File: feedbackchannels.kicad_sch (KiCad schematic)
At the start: 75 parts

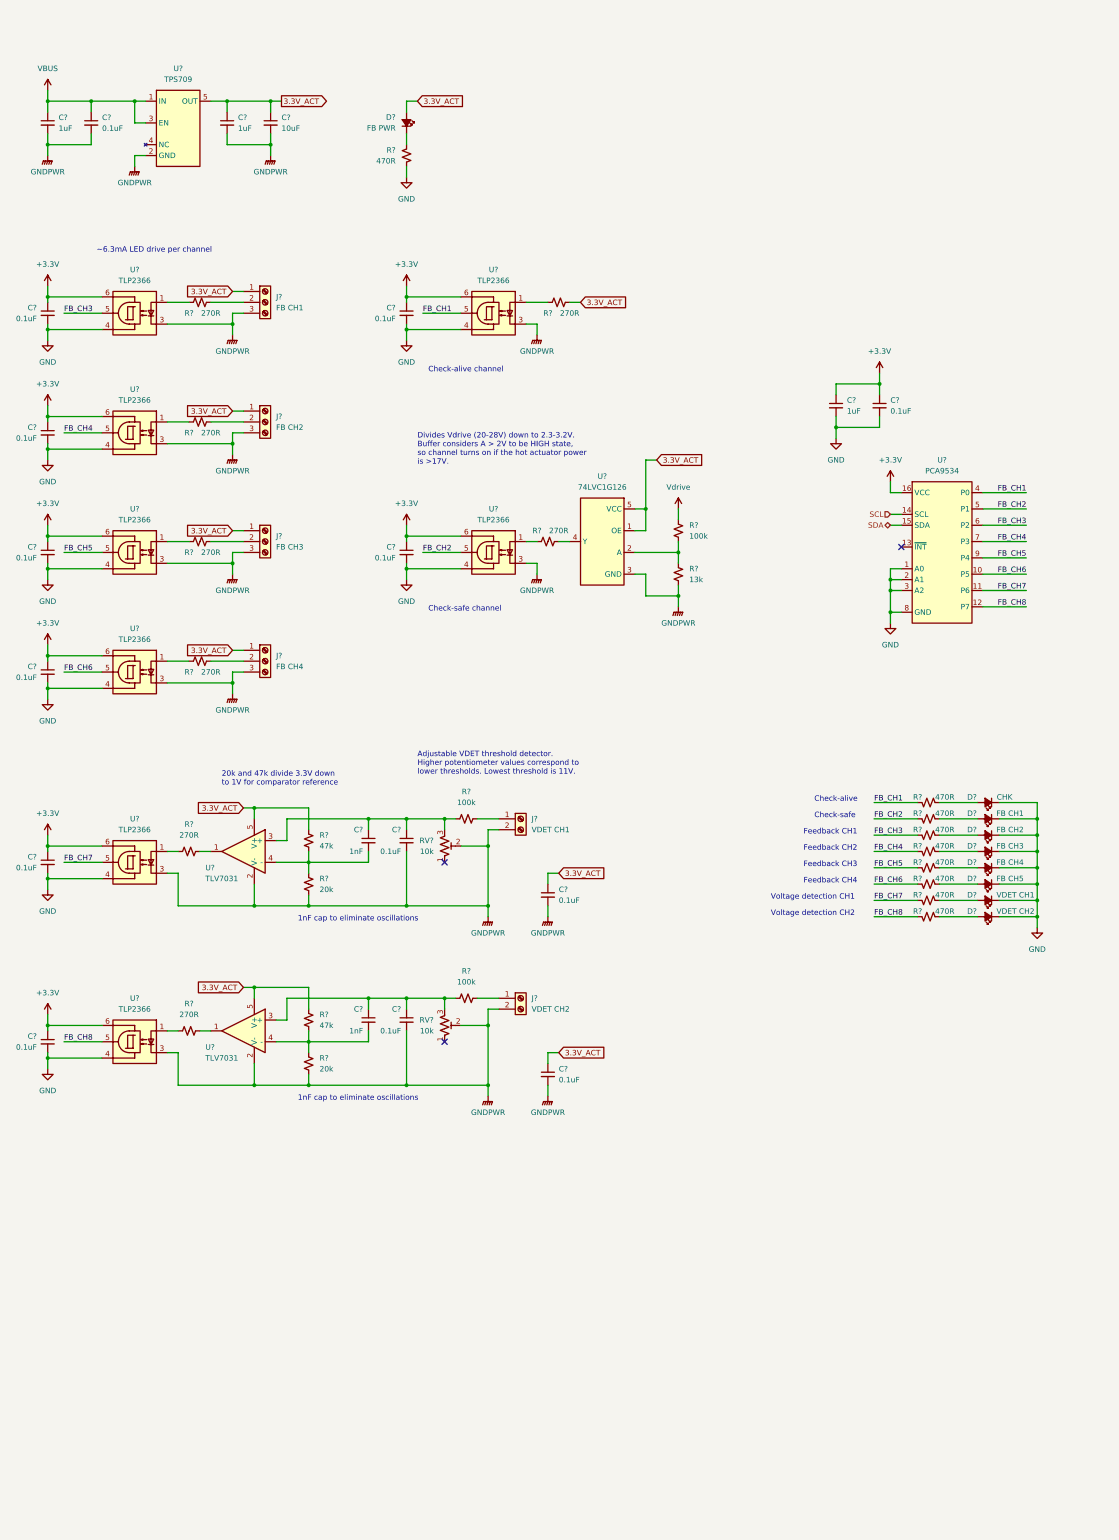
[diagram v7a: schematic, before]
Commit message: Added hot-side supply protection
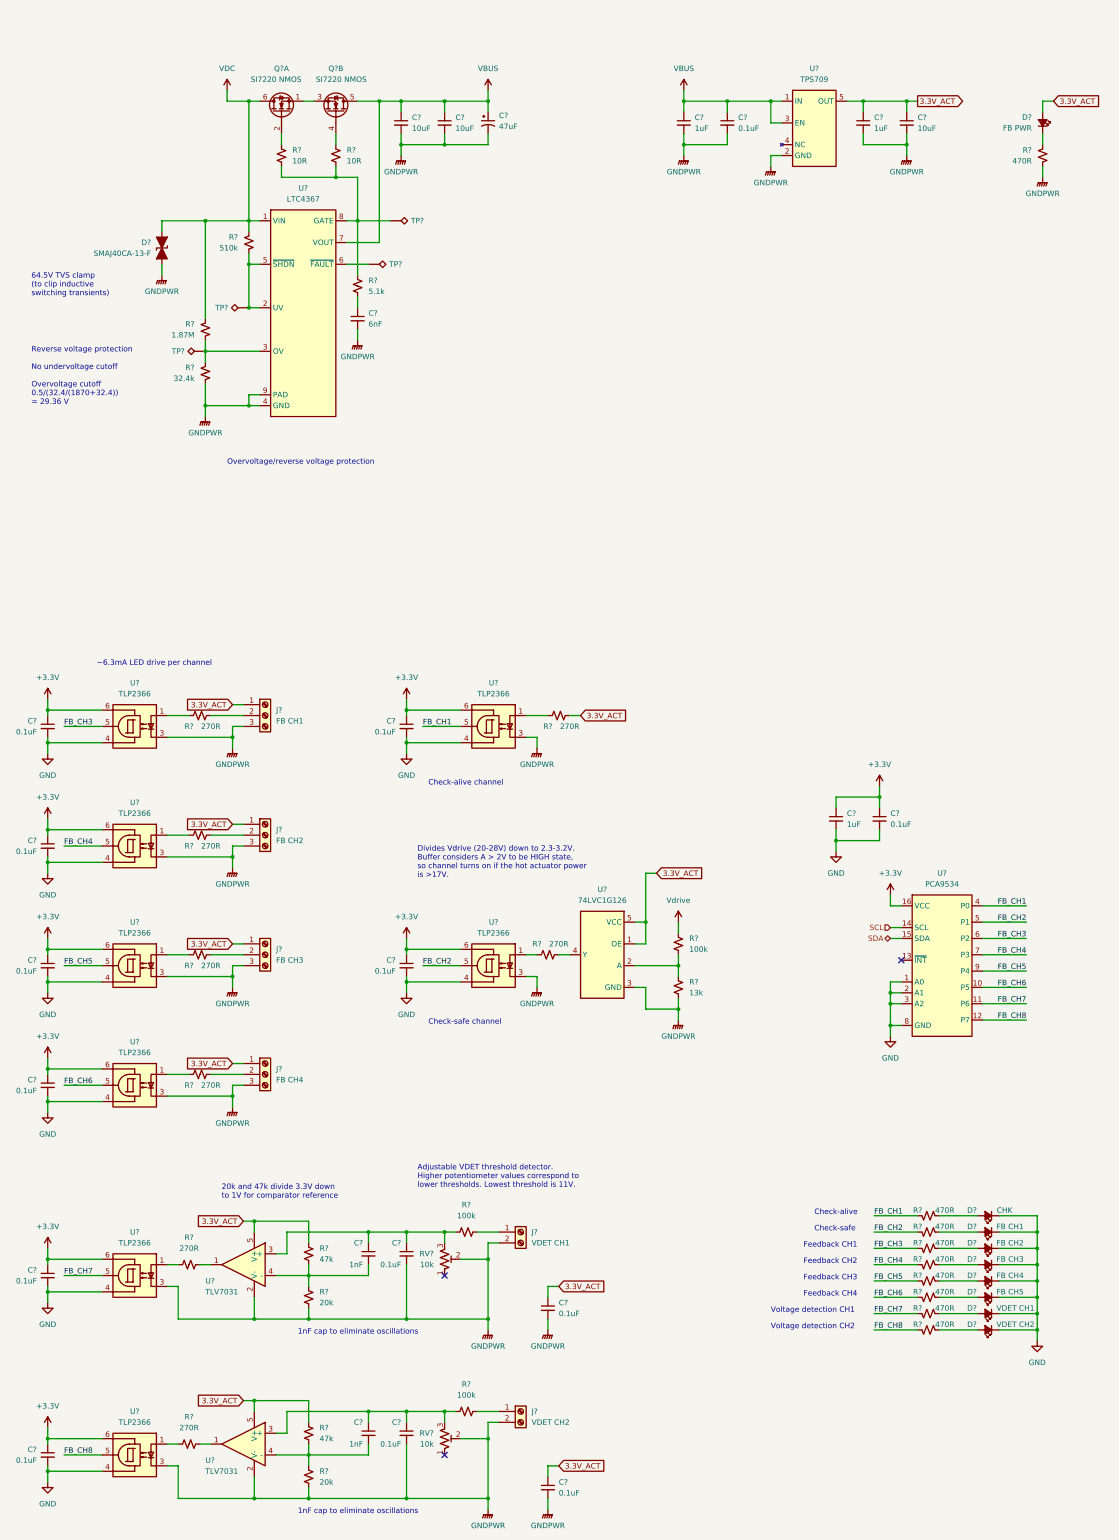
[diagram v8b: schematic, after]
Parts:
- added C? (x2): 10uF, Capacitor_SMD:C_1206_3216Metric, symbol Device:C_Small
- added C?: 47uF, Capacitor_SMD:CP_Elec_8x6.2, symbol Device:C_Polarized_Small_US
- added C?: 6nF, Capacitor_SMD:C_0603_1608Metric, symbol Device:C_Small
- added D?: SMAJ40CA-13-F, Diode_SMD:D_SMA, symbol Device:D_TVS_Filled
- added Q? (x2): SI7220 NMOS, Package_SO:Vishay_PowerPAK_1212-8_Dual, symbol Device:Q_Dual_NMOS_S1G1S2G2D2D2D1D1
- added R? (x2): 10R, Resistor_SMD:R_0603_1608Metric, symbol Device:R_Small_US
- added R?: 1.87M, Resistor_SMD:R_0603_1608Metric, symbol Device:R_Small_US
- added R?: 510k, Resistor_SMD:R_0603_1608Metric, symbol Device:R_Small_US
- added R?: 5.1k, Resistor_SMD:R_0603_1608Metric, symbol Device:R_Small_US
- added R?: 32.4k, Resistor_SMD:R_0603_1608Metric, symbol Device:R_Small_US
- added TP? (x4): TestPoint_Alt, TestPoint:TestPoint_Pad_D2.0mm, symbol Connector:TestPoint_Alt
- added U?: LTC4367, Package_DFN_QFN:DFN-8-1EP_3x3mm_P0.5mm_EP1.65x2.38mm, symbol interface:LTC4367
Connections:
- net GND: no longer R?.2
- net GNDPWR: now also R?.2, C?.2, C?.2, C?.2, C?.2, D?.1 (A1), R?.1, U?.4 (GND), U?.9 (PAD)
- net VBUS: now also C?.1, C?.1, C?.1, Q?.5 (D), U?.7 (VOUT)
- new net: TP?.1, U?.6 (~{FAULT})
- new net: R?.1, R?.2, TP?.1, U?.3 (OV)
- new net: R?.1, TP?.1, U?.2 (UV), U?.5 (~{SHDN})
- new net: Q?.4 (G), R?.1
- new net: R?.1, R?.2, R?.2, TP?.1, U?.8 (GATE)
- new net: Q?.1 (S), Q?.3 (S)
- new net: Q?.2 (G), R?.1
- new net: C?.1, R?.2
- new net VDC: D?.2 (A2), Q?.6 (D), R?.2, R?.2, U?.1 (VIN)
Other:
- note added: "64.5V TVS clamp (to clip inductive switching transients)"
- note added: "Overvoltage/reverse voltage protection"
- note added: "Reverse voltage protection No undervoltage cutoff Overvoltage cutoff 0.5/(32.4/(1870+32.4)) = 29.36 V"
- moved on the sheet: C?, D?, J?, R?, RV?, U?
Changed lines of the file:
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@@
 (kicad_sch (version 20211123) (generator eeschema)
-  (paper "User" 299.999 299.999)
+  (paper "User" 299.999 399.999)
